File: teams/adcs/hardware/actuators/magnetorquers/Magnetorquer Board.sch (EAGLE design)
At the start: 24 parts

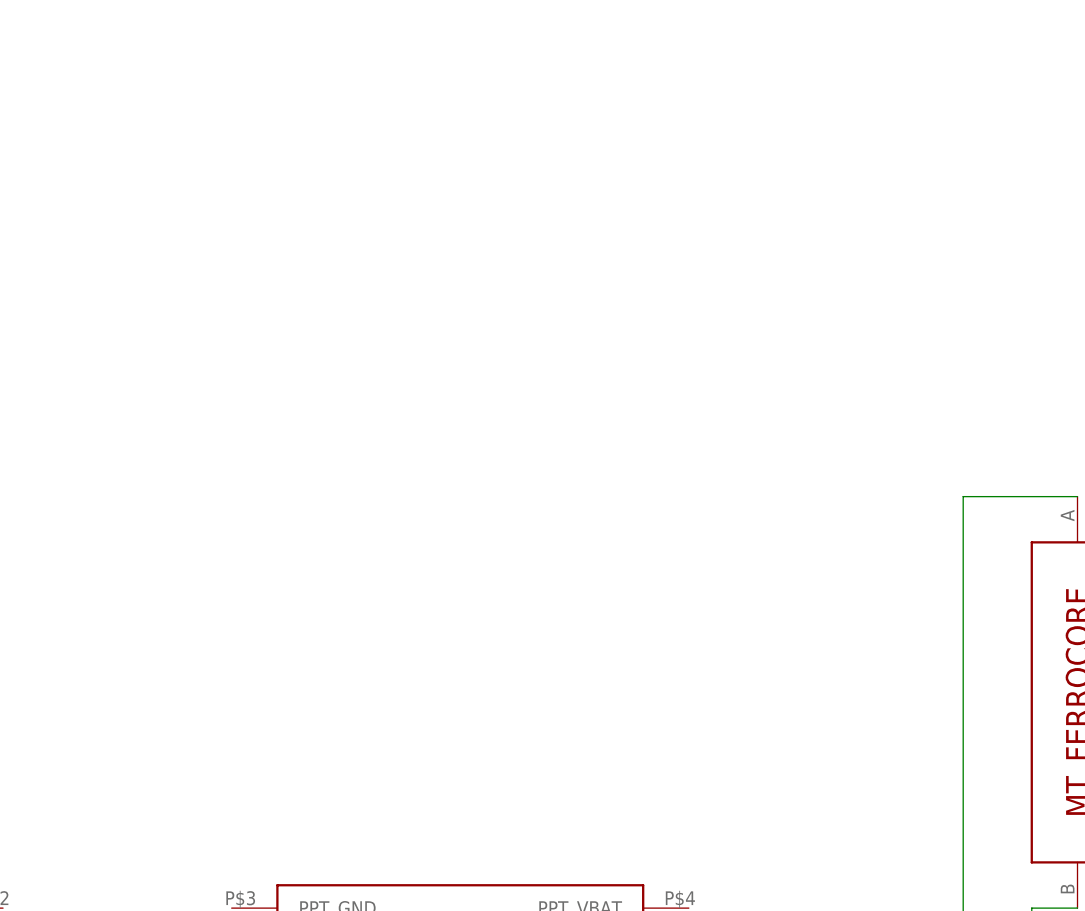
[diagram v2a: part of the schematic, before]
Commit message: ADCS/MT: Start building SEPIC converter topology
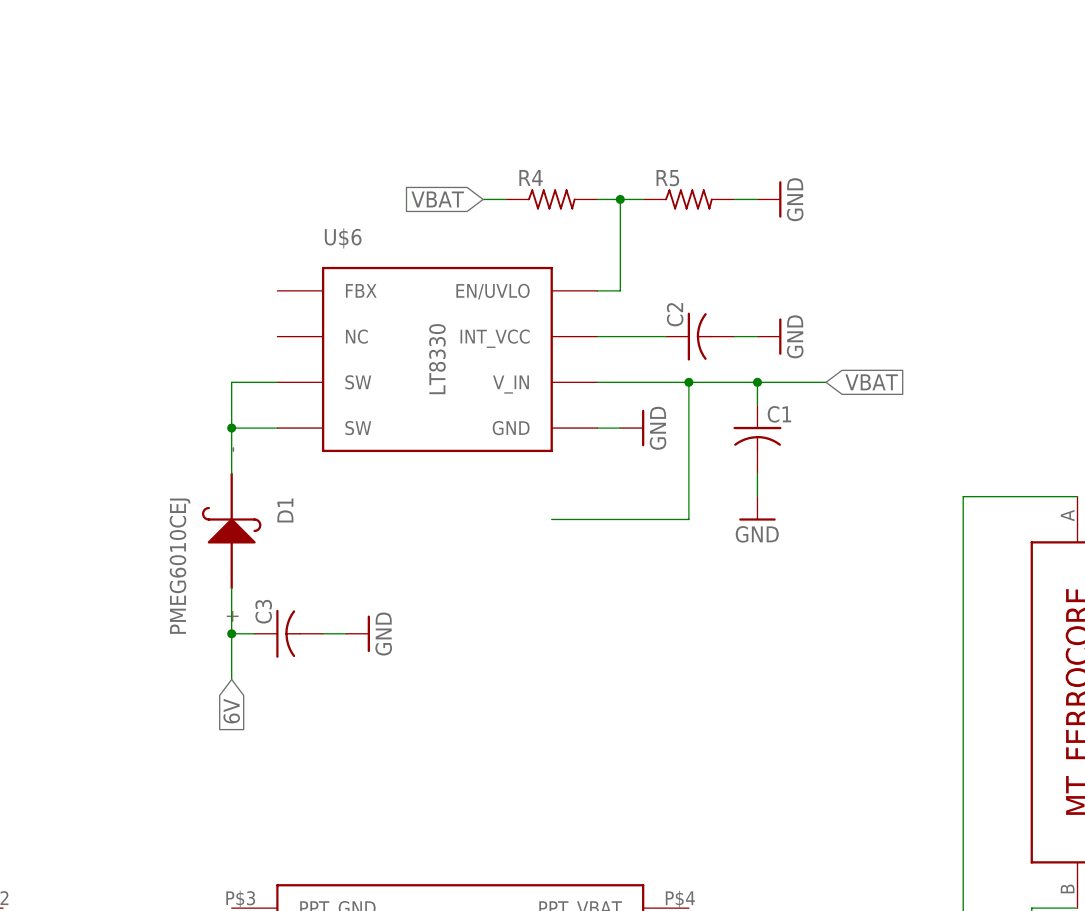
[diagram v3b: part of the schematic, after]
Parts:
- added C1, C2, C3: (no value), rcl:C-USC0805
- added D1: PMEG6010CEJ, DubSat1 Components:PMEG6010CEJ
- added R4, R5: (no value), rcl:R-US_R0805
- added U$6: LT8330, DubSat1 Components:LT8330
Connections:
- new net N$3: D1.-, U$6.SW@1, U$6.SW@2
- new net N$4: C2.1, U$6.INT_VCC
- new net N$5: R4.2, R5.1, U$6.EN/UVLO
- net 6V: now also C3.1, D1.+
- net GND: now also C1.2, C2.2, C3.2, R5.2, U$6.GND
- net VBAT: now also C1.1, R4.1, U$6.V_IN
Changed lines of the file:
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@@
 <part name="GND19" library="supply1" library_urn="urn:adsk.eagle:library:371" deviceset="GND" device=""/>
 <part name="GND20" library="supply1" library_urn="urn:adsk.eagle:library:371" deviceset="GND" device=""/>
+<part name="U$6" library="DubSat1 Components" deviceset="LT8330" device=""/>
+<part name="GND7" library="supply1" library_urn="urn:adsk.eagle:library:371" deviceset="GND" device=""/>
+<part name="C1" library="rcl" library_urn="urn:adsk.eagle:library:334" deviceset="C-US" device="C0805" package3d_urn="urn:adsk.eagle:package:23617/2"/>
+<part name="GND10" library="supply1" library_urn="urn:adsk.eagle:library:371" deviceset="GND" device=""/>
+<part name="C2" library="rcl" library_urn="urn:adsk.eagle:library:334" deviceset="C-US" device="C0805" package3d_urn="urn:adsk.eagle:package:23617/2"/>
+<part name="GND11" library="supply1" library_urn="urn:adsk.eagle:library:371" deviceset="GND" device=""/>
+<part name="R4" library="rcl" library_urn="urn:adsk.eagle:library:334" deviceset="R-US_" device="R0805" package3d_urn="urn:adsk.eagle:package:23553/2"/>
+<part name="R5" library="rcl" library_urn="urn:adsk.eagle:library:334" deviceset="R-US_" device="R0805" package3d_urn="urn:adsk.eagle:package:23553/2"/>
+<part name="GND14" library="supply1" library_urn="urn:adsk.eagle:library:371" deviceset="GND" device=""/>
+<part name="D1" library="DubSat1 Components" deviceset="PMEG6010CEJ" device=""/>
+<part name="C3" library="rcl" library_urn="urn:adsk.eagle:library:334" deviceset="C-US" device="C0805" package3d_urn="urn:adsk.eagle:package:23617/2"/>
+<part name="GND21" library="supply1" library_urn="urn:adsk.eagle:library:371" deviceset="GND" device=""/>
 </parts>
 <sheets>
@@
 <instance part="GND19" gate="1" x="-12.7" y="185.42" rot="R90"/>
 <instance part="GND20" gate="1" x="17.78" y="185.42" rot="R90"/>
+<instance part="U$6" gate="G$1" x="78.74" y="147.32"/>
+<instance part="GND7" gate="1" x="101.6" y="139.7" rot="R90"/>
+<instance part="C1" gate="G$1" x="114.3" y="139.7"/>
+<instance part="GND10" gate="1" x="114.3" y="129.54"/>
+<instance part="C2" gate="G$1" x="106.68" y="149.86" rot="R90"/>
+<instance part="GND11" gate="1" x="116.84" y="149.86" rot="R90"/>
+<instance part="R4" gate="G$1" x="91.44" y="165.1"/>
+<instance part="R5" gate="G$1" x="106.68" y="165.1"/>
+<instance part="GND14" gate="1" x="116.84" y="165.1" rot="R90"/>
+<instance part="D1" gate="G$1" x="55.88" y="129.54" rot="R270"/>
+<instance part="C3" gate="G$1" x="60.96" y="116.84" rot="R90"/>
+<instance part="GND21" gate="1" x="71.12" y="116.84" rot="R90"/>
 </instances>
 <busses>
@@
 <pinref part="GND20" gate="1" pin="GND"/>
 <wire x1="12.7" y1="185.42" x2="15.24" y2="185.42" width="0.1524" layer="91"/>
+</segment>
+<segment>
+<pinref part="U$6" gate="G$1" pin="GND"/>
+<pinref part="GND7" gate="1" pin="GND"/>
+<wire x1="96.52" y1="139.7" x2="99.06" y2="139.7" width="0.1524" layer="91"/>
+</segment>
+<segment>
+<pinref part="C1" gate="G$1" pin="2"/>
+<pinref part="GND10" gate="1" pin="GND"/>
+<wire x1="114.3" y1="134.62" x2="114.3" y2="132.08" width="0.1524" layer="91"/>
+</segment>
+<segment>
+<pinref part="C2" gate="G$1" pin="2"/>
+<pinref part="GND11" gate="1" pin="GND"/>
+<wire x1="114.3" y1="149.86" x2="111.76" y2="149.86" width="0.1524" layer="91"/>
+</segment>
+<segment>
+<pinref part="R5" gate="G$1" pin="2"/>
+<pinref part="GND14" gate="1" pin="GND"/>
+<wire x1="111.76" y1="165.1" x2="114.3" y2="165.1" width="0.1524" layer="91"/>
+</segment>
+<segment>
+<pinref part="C3" gate="G$1" pin="2"/>
+<pinref part="GND21" gate="1" pin="GND"/>
+<wire x1="68.58" y1="116.84" x2="66.04" y2="116.84" width="0.1524" layer="91"/>
 </segment>
 </net>
@@
 <junction x="152.4" y="53.34"/>
 </segment>
+<segment>
+<pinref part="D1" gate="G$1" pin="+"/>
+<wire x1="55.88" y1="121.92" x2="55.88" y2="116.84" width="0.1524" layer="91"/>
+<pinref part="C3" gate="G$1" pin="1"/>
+<wire x1="55.88" y1="116.84" x2="58.42" y2="116.84" width="0.1524" layer="91"/>
+<wire x1="55.88" y1="116.84" x2="55.88" y2="111.76" width="0.1524" layer="91"/>
+<junction x="55.88" y="116.84"/>
+<label x="55.88" y="111.76" size="1.778" layer="95" rot="R270" xref="yes"/>
+</segment>
 </net>
 <net name="VBAT" class="0">
@@
 <wire x1="55.88" y1="33.02" x2="50.8" y2="33.02" width="0.1524" layer="91"/>
 <label x="50.8" y="33.02" size="1.778" layer="95" rot="R180" xref="yes"/>
+</segment>
+<segment>
+<pinref part="U$6" gate="G$1" pin="V_IN"/>
+<label x="121.92" y="144.78" size="1.778" layer="95" xref="yes"/>
+<pinref part="C1" gate="G$1" pin="1"/>
+<wire x1="96.52" y1="144.78" x2="106.68" y2="144.78" width="0.1524" layer="91"/>
+<wire x1="106.68" y1="144.78" x2="114.3" y2="144.78" width="0.1524" layer="91"/>
+<wire x1="114.3" y1="144.78" x2="121.92" y2="144.78" width="0.1524" layer="91"/>
+<wire x1="114.3" y1="144.78" x2="114.3" y2="142.24" width="0.1524" layer="91"/>
+<junction x="114.3" y="144.78"/>
+<wire x1="106.68" y1="144.78" x2="106.68" y2="129.54" width="0.1524" layer="91"/>
+<junction x="106.68" y="144.78"/>
+<wire x1="106.68" y1="129.54" x2="91.44" y2="129.54" width="0.1524" layer="91"/>
+</segment>
+<segment>
+<pinref part="R4" gate="G$1" pin="1"/>
+<wire x1="86.36" y1="165.1" x2="83.82" y2="165.1" width="0.1524" layer="91"/>
+<label x="83.82" y="165.1" size="1.778" layer="95" rot="R180" xref="yes"/>
 </segment>
 </net>
@@
 </segment>
 </net>
+<net name="N$4" class="0">
+<segment>
+<pinref part="U$6" gate="G$1" pin="INT_VCC"/>
+<wire x1="96.52" y1="149.86" x2="104.14" y2="149.86" width="0.1524" layer="91"/>
+<pinref part="C2" gate="G$1" pin="1"/>
+</segment>
+</net>
+<net name="N$5" class="0">
+<segment>
+<pinref part="U$6" gate="G$1" pin="EN/UVLO"/>
+<wire x1="96.52" y1="154.94" x2="99.06" y2="154.94" width="0.1524" layer="91"/>
+<wire x1="99.06" y1="154.94" x2="99.06" y2="165.1" width="0.1524" layer="91"/>
+<pinref part="R5" gate="G$1" pin="1"/>
+<wire x1="99.06" y1="165.1" x2="101.6" y2="165.1" width="0.1524" layer="91"/>
+<pinref part="R4" gate="G$1" pin="2"/>
+<wire x1="99.06" y1="165.1" x2="96.52" y2="165.1" width="0.1524" layer="91"/>
+<junction x="99.06" y="165.1"/>
+</segment>
+</net>
+<net name="N$3" class="0">
+<segment>
+<pinref part="U$6" gate="G$1" pin="SW@1"/>
+<pinref part="D1" gate="G$1" pin="-"/>
+<wire x1="60.96" y1="144.78" x2="55.88" y2="144.78" width="0.1524" layer="91"/>
+<wire x1="55.88" y1="144.78" x2="55.88" y2="139.7" width="0.1524" layer="91"/>
+<pinref part="U$6" gate="G$1" pin="SW@2"/>
+<wire x1="55.88" y1="139.7" x2="55.88" y2="134.62" width="0.1524" layer="91"/>
+<wire x1="60.96" y1="139.7" x2="55.88" y2="139.7" width="0.1524" layer="91"/>
+<junction x="55.88" y="139.7"/>
+</segment>
+</net>

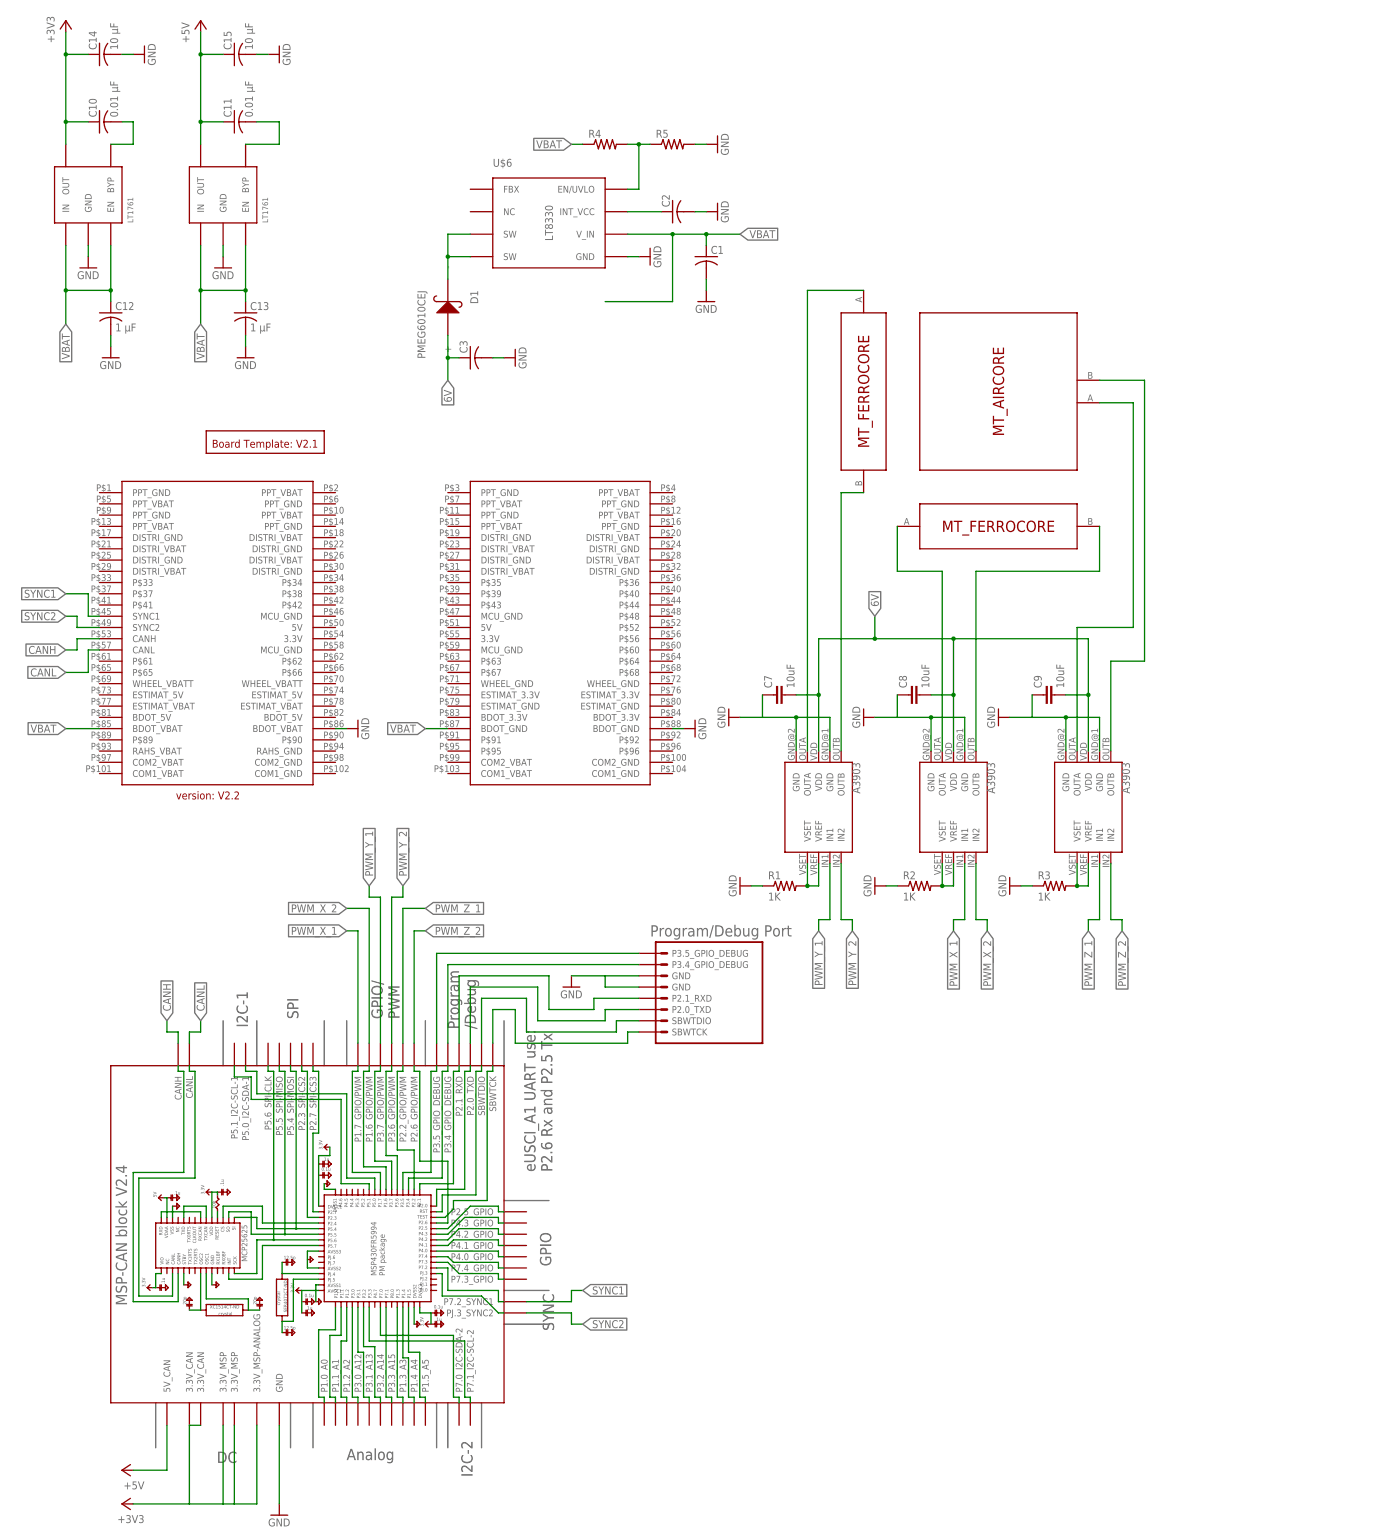
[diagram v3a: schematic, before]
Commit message: ADCS/MT: Rerouted with new power converter
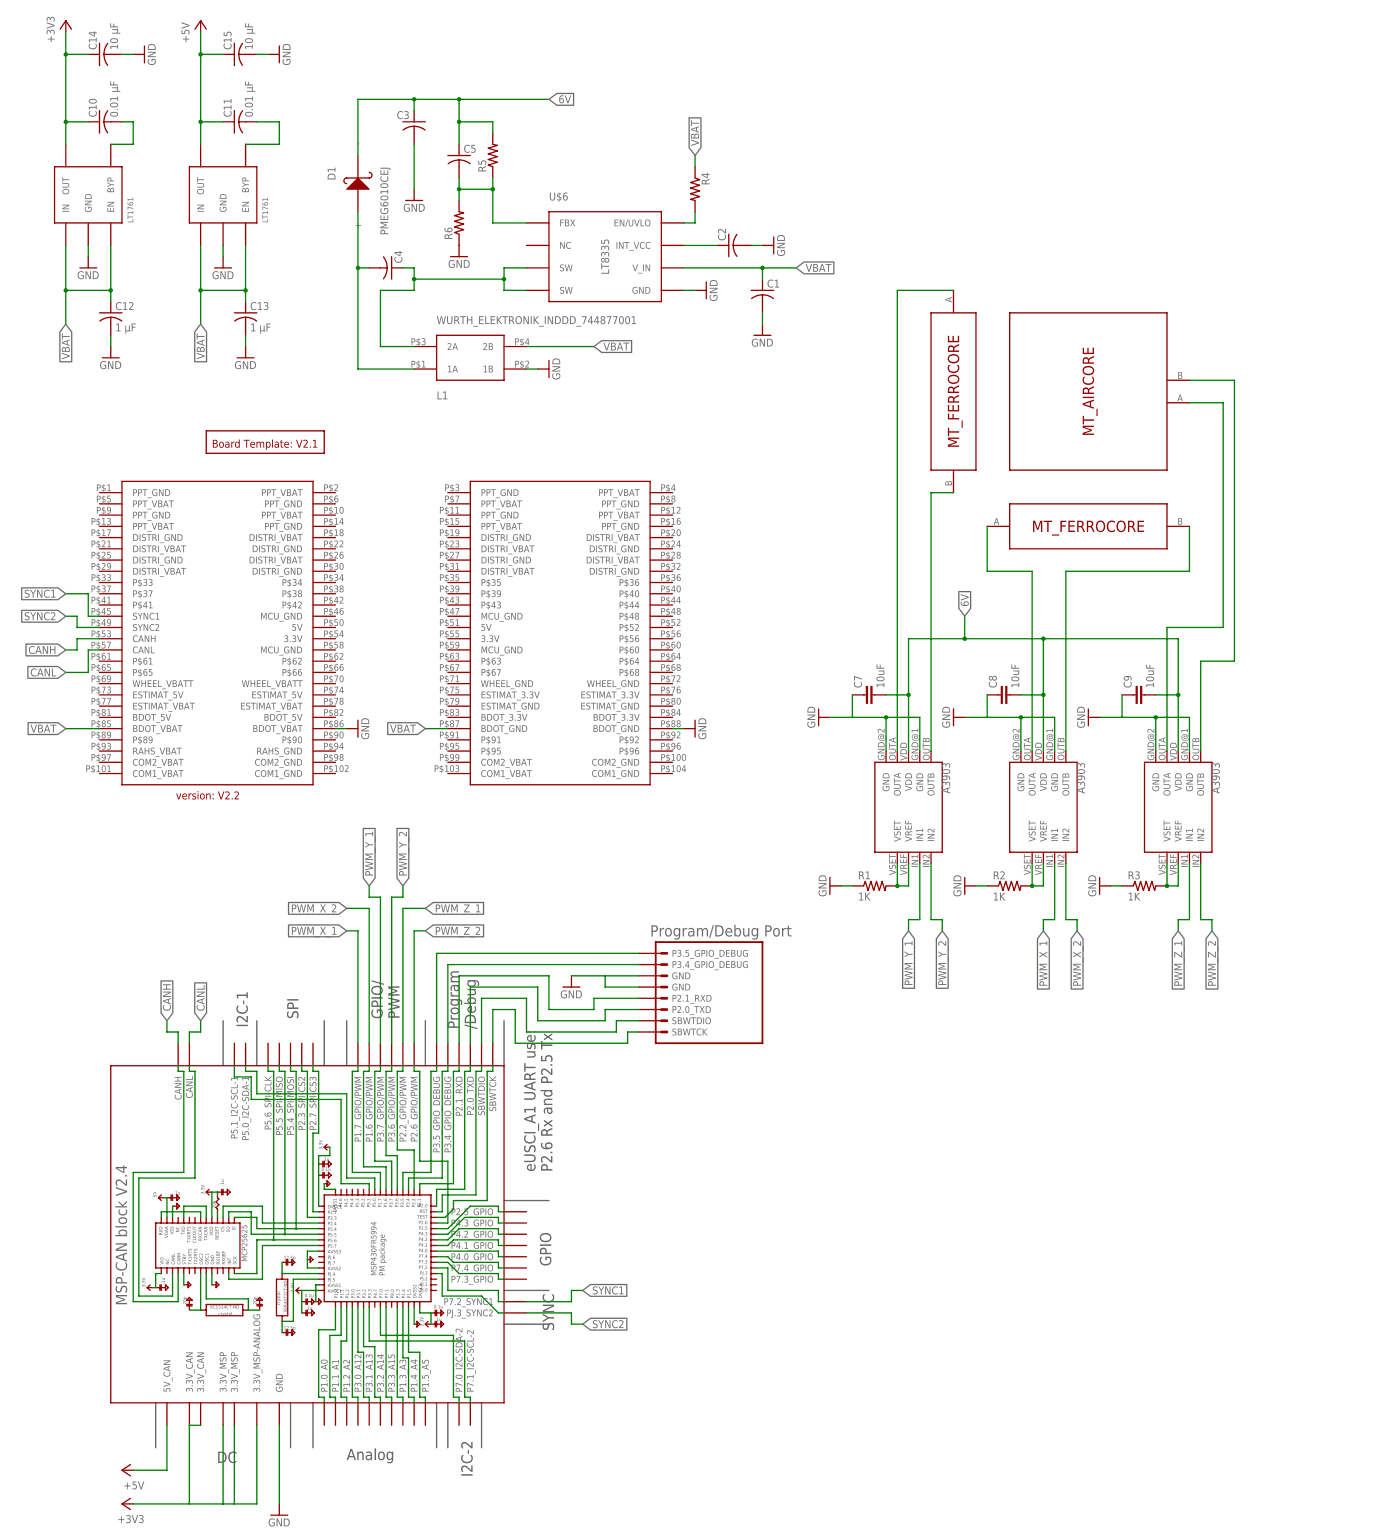
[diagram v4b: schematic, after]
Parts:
- added C4, C5: (no value), rcl:C-USC0805
- added L1: WURTH_ELEKTRONIK_INDDD_744877001, DubSat1 Components:WURTH_ELEKTRONIK_INDDD_744877001
- added R6: (no value), rcl:R-US_R0805
- U$6: value LT8330 -> LT8335; device DubSat1 Components:LT8330 -> DubSat1 Components:LT8335
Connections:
- net N$4 renamed INT_VCC
- removed net N$3: D1.-, U$6.SW@1, U$6.SW@2
- removed net N$5: R4.2, R5.1, U$6.EN/UVLO
- new net EN_UVLO: R4.2, U$6.EN/UVLO
- new net FBX: C5.2, R5.1, R6.2, U$6.FBX
- new net N$6: C4.2, D1.+, L1.1A
- new net SW: C4.1, L1.2A, U$6.SW@1, U$6.SW@2
- net 6V: now also C5.1, D1.-, R5.2; no longer D1.+
- net GND: now also L1.1B, R6.1; no longer R5.2
- net VBAT: now also L1.2B
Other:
- moved on the sheet: C1, C2, C3, C7, C8, C9, D1, R1, R2, R3, R4, R5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
